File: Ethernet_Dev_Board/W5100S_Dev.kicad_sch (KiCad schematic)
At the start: 41 parts, among them U5 74AUP1T08GWH, Y1 25MHz

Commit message: Added in ESP circuit
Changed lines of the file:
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@@
+		)
+	)
+	(text_box "Will need to check if W5100S regulator comes on if chip does not have clock source"
+		(exclude_from_sim no)
+		(at 66.04 175.26 0)
+		(size 25.4 19.05)
+		(stroke
+			(width 0)
+			(type default)
+		)
+		(fill
+			(type none)
+		)
+		(effects
+			(font
+				(size 1.27 1.27)
+			)
+			(justify left top)
 		)
 	)

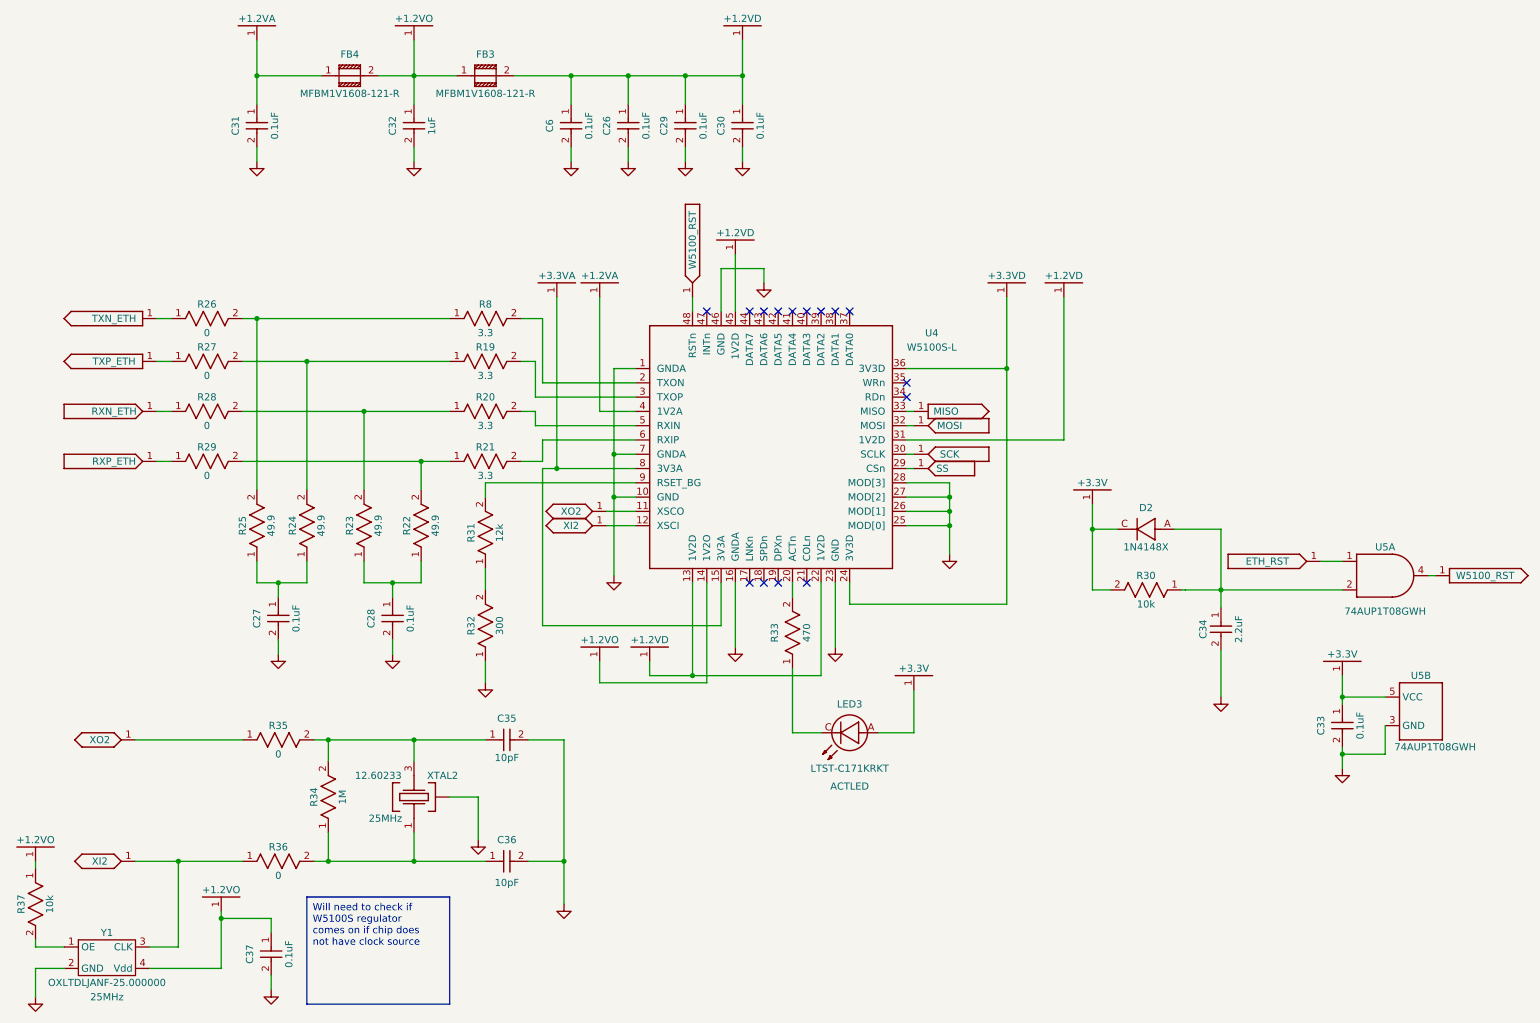
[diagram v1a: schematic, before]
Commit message: Added additional oscillator circuit. Re-annotated schematic
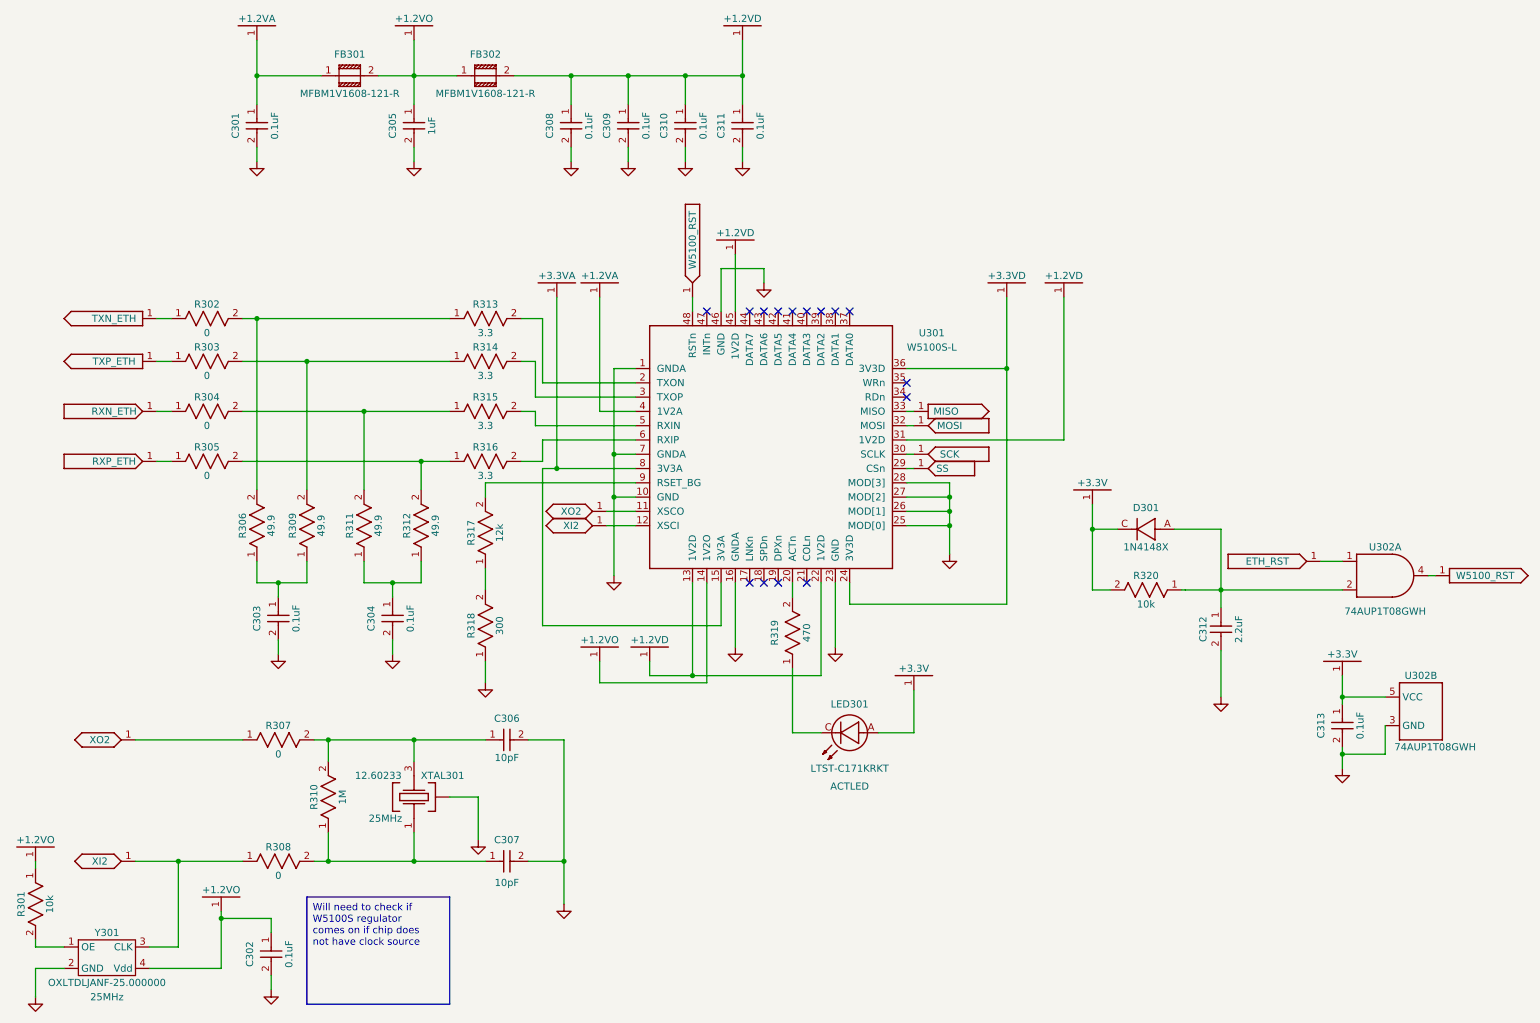
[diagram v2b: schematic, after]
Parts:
- renumbered C31 to C301, C37 to C302, C27 to C303, C28 to C304, C32 to C305, C35 to C306, C36 to C307, C6 to C308, C26 to C309, C29 to C310, C30 to C311, C34 to C312, C33 to C313, D2 to D301, FB4 to FB301, FB3 to FB302, LED3 to LED301, R37 to R301, R26 to R302, R27 to R303, R28 to R304, R29 to R305, R25 to R306, R35 to R307, R36 to R308, R24 to R309, R34 to R310, R23 to R311, R22 to R312, R8 to R313, R19 to R314, R20 to R315, R21 to R316, R31 to R317, R32 to R318, R33 to R319, R30 to R320, U4 to U301, U5 to U302, XTAL2 to XTAL301, Y1 to Y301
